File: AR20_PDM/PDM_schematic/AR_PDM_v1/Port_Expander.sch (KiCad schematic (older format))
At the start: 3 parts

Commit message: Fixed issues, controlled components, BOM, see discription
- added acm symbol
- fixed wrongly faced P-mosfets
- I/O expander now sinks led instead of source
- Bill of material mostly done
- Correct address for INA233 chips.
- Now 4 diodes serves as flyback for all mosfets
- Corrected naming scheme for compmonents (everything is not fixed yet)
- Fixed some labels
- altso some minor changes
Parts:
- added C_bypass10, C_bypass9: 100nf, Capacitor_SMD:C_0603_1608Metric, symbol AR20_PDM_v1-rescue:C-Device
- Pullup1, Pullup2: renamed from Pullup?; value 4.7K -> 4K7
- gave numbers to parts that had none: 1
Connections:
- net labels removed: EXPANDER_INT
- wire segments 4 -> 8
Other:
- note added: "Close to PIN"
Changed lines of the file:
@@
 $Descr A4 11693 8268
 encoding utf-8
-Sheet 13 13
+Sheet 12 13
 Title ""
 Date ""
@@
 Comment4 ""
 $EndDescr
-Text HLabel 4000 4075 0    50   Output ~ 0
+Text HLabel 4000 4075 0    50   Input ~ 0
 COIL_INJECTOR_Fault
-Text HLabel 4750 4875 2    50   Output ~ 0
+Text HLabel 4750 4875 2    50   Input ~ 0
 FUEL_PUMP_Fault
-Text HLabel 4000 4775 0    50   Output ~ 0
+Text HLabel 4000 4775 0    50   Input ~ 0
 P7_Fault
-Text HLabel 4000 4675 0    50   Output ~ 0
+Text HLabel 4000 4675 0    50   Input ~ 0
 P6_Fault
-Text HLabel 4000 4575 0    50   Output ~ 0
+Text HLabel 4000 4575 0    50   Input ~ 0
 P5_Fault
-Text HLabel 4000 4475 0    50   Output ~ 0
+Text HLabel 4000 4475 0    50   Input ~ 0
 P4_Fault
-Text HLabel 4000 4375 0    50   Output ~ 0
+Text HLabel 4000 4375 0    50   Input ~ 0
 P3_Fault
-Text HLabel 4000 4175 0    50   Output ~ 0
+Text HLabel 4000 4175 0    50   Input ~ 0
 P1_Fault
-Text HLabel 4000 4275 0    50   Output ~ 0
+Text HLabel 4000 4275 0    50   Input ~ 0
 P2_Fault
 Text HLabel 4750 4775 2    50   Output ~ 0
@@
 AR Path="/5DE4D361/5E218A64" Ref="#PWR?"  Part="1"
 AR Path="/5E218A64" Ref="#PWR?"  Part="1"
-AR Path="/5E1AEC18/5E218A64" Ref="#PWR?"  Part="1"
-F 0 "#PWR?" H 4000 4625 50  0001 C CNN
+AR Path="/5E1AEC18/5E218A64" Ref="#PWR091"  Part="1"
+F 0 "#PWR091" H 4000 4625 50  0001 C CNN
 F 1 "GND" V 4000 4675 50  0000 C CNN
 F 2 "" H 4000 4875 50  0001 C CNN
@@
 Text HLabel 4750 3875 2    50   Input ~ 0
 SDA
-Text HLabel 4750 3775 2    50   Input ~ 0
-VCC_5v
-$Comp
-L AR20_PDM_v1-rescue:TCA6416A-PortExpander U?
+Text HLabel 5025 3775 2    50   Input ~ 0
+VCC_5v
+$Comp
+L AR20_PDM_v1-rescue:TCA6416A-PortExpander U12
 U 1 1 5E21A7B6
 P 4350 5025
-F 0 "U?" H 4375 6500 50  0000 C CNN
+F 0 "U12" H 4375 6500 50  0000 C CNN
 F 1 "TCA6416A-PortExpander" H 4375 6409 50  0000 C CNN
 F 2 "" H 4350 5025 50  0001 C CNN
@@
 VCC_5v
 $Comp
-L AR20_PDM_v1-rescue:R-Device R_s?
+L AR20_PDM_v1-rescue:R-Device Pullup?
 U 1 1 5E2206AE
 P 3875 3625
-AR Path="/5DA89415/5E2206AE" Ref="R_s?"  Part="1"
-AR Path="/5DA8920B/5E2206AE" Ref="R_s?"  Part="1"
-AR Path="/5E2546F2/5E2206AE" Ref="R_s?"  Part="1"
-AR Path="/5E1AEC18/5E2206AE" Ref="Pullup?"  Part="1"
-F 0 "Pullup?" V 3668 3625 50  0000 C CNN
-F 1 "4.7K" V 3759 3625 50  0000 C CNN
+AR Path="/5DA89415/5E2206AE" Ref="Pullup?"  Part="1"
+AR Path="/5DA8920B/5E2206AE" Ref="Pullup?"  Part="1"
+AR Path="/5E2546F2/5E2206AE" Ref="Pullup?"  Part="1"
+AR Path="/5E1AEC18/5E2206AE" Ref="Pullup2"  Part="1"
+F 0 "Pullup2" V 3668 3625 50  0000 C CNN
+F 1 "4K7" V 3759 3625 50  0000 C CNN
 F 2 "" V 3805 3625 50  0001 C CNN
 F 3 "~" H 3875 3625 50  0001 C CNN
@@
 Wire Wire Line
 	4000 3775 3875 3775
-Connection ~ 3875 3775
-Text HLabel 4000 3875 0    50   Input ~ 0
+Text HLabel 2575 3875 0    50   Input ~ 0
 VCC_5v
 Text HLabel 3575 3450 1    50   Input ~ 0
@@
 AR Path="/5DA8920B/5E228956" Ref="Pullup?"  Part="1"
 AR Path="/5E2546F2/5E228956" Ref="Pullup?"  Part="1"
-AR Path="/5E1AEC18/5E228956" Ref="Pullup?"  Part="1"
-F 0 "Pullup?" V 3368 3600 50  0000 C CNN
-F 1 "4.7K" V 3459 3600 50  0000 C CNN
+AR Path="/5E1AEC18/5E228956" Ref="Pullup1"  Part="1"
+F 0 "Pullup1" V 3368 3600 50  0000 C CNN
+F 1 "4K7" V 3459 3600 50  0000 C CNN
 F 2 "" V 3505 3600 50  0001 C CNN
 F 3 "~" H 3575 3600 50  0001 C CNN
@@
 Wire Wire Line
 	3575 3975 4000 3975
-Wire Wire Line
-	3200 3775 3875 3775
-Text HLabel 3200 3775 0    50   Input ~ 0
-EXPANDER_INT
 Text Notes 5150 3950 0    50   ~ 0
 ADDR to gnd, i2c Address: 0100000
@@
 AR Path="/5DE4D361/5E22B252" Ref="#PWR?"  Part="1"
 AR Path="/5E22B252" Ref="#PWR?"  Part="1"
-AR Path="/5E1AEC18/5E22B252" Ref="#PWR?"  Part="1"
-F 0 "#PWR?" H 4750 3825 50  0001 C CNN
+AR Path="/5E1AEC18/5E22B252" Ref="#PWR092"  Part="1"
+F 0 "#PWR092" H 4750 3825 50  0001 C CNN
 F 1 "GND" V 4750 3875 50  0000 C CNN
 F 2 "" H 4750 4075 50  0001 C CNN
@@
 	0    -1   -1   0
 $EndComp
+$Comp
+L AR20_PDM_v1-rescue:C-Device C_bypass?
+U 1 1 5E21FC4A
+P 2600 4100
+AR Path="/5DA89415/5E21FC4A" Ref="C_bypass?"  Part="1"
+AR Path="/5DEB10A1/5E21FC4A" Ref="C_bypass?"  Part="1"
+AR Path="/5DEB20EA/5E21FC4A" Ref="C_bypass?"  Part="1"
+AR Path="/5E0E4725/5E21FC4A" Ref="C_bypass?"  Part="1"
+AR Path="/5E0E4A93/5E21FC4A" Ref="C_bypass?"  Part="1"
+AR Path="/5E0E4EB5/5E21FC4A" Ref="C_bypass?"  Part="1"
+AR Path="/5E0E5304/5E21FC4A" Ref="C_bypass?"  Part="1"
+AR Path="/5E0E594B/5E21FC4A" Ref="C_bypass?"  Part="1"
+AR Path="/5E0E607C/5E21FC4A" Ref="C_bypass?"  Part="1"
+AR Path="/5E0FB5C8/5E21FC4A" Ref="C_bypass?"  Part="1"
+AR Path="/5E0FBBBD/5E21FC4A" Ref="C_bypass?"  Part="1"
+AR Path="/5E0FC3A2/5E21FC4A" Ref="C_bypass?"  Part="1"
+AR Path="/5E0FCFDC/5E21FC4A" Ref="C_bypass?"  Part="1"
+AR Path="/5E0FDCCC/5E21FC4A" Ref="C_bypass?"  Part="1"
+AR Path="/5E10174B/5E21FC4A" Ref="C_bypass?"  Part="1"
+AR Path="/5E1AEC18/5E21FC4A" Ref="C_bypass9"  Part="1"
+F 0 "C_bypass9" V 2348 4100 50  0000 C CNN
+F 1 "100nf" V 2439 4100 50  0000 C CNN
+F 2 "Capacitor_SMD:C_0603_1608Metric" H 2638 3950 50  0001 C CNN
+F 3 "~" H 2600 4100 50  0001 C CNN
+	1    2600 4100
+	1    0    0    -1
+$EndComp
+$Comp
+L AR20_PDM_v1-rescue:GND-power #PWR?
+U 1 1 5E21FC50
+P 2600 4250
+AR Path="/5DA89415/5E21FC50" Ref="#PWR?"  Part="1"
+AR Path="/5DEB10A1/5E21FC50" Ref="#PWR?"  Part="1"
+AR Path="/5DEB20EA/5E21FC50" Ref="#PWR?"  Part="1"
+AR Path="/5E0E4725/5E21FC50" Ref="#PWR?"  Part="1"
+AR Path="/5E0E4A93/5E21FC50" Ref="#PWR?"  Part="1"
+AR Path="/5E0E4EB5/5E21FC50" Ref="#PWR?"  Part="1"
+AR Path="/5E0E5304/5E21FC50" Ref="#PWR?"  Part="1"
+AR Path="/5E0E594B/5E21FC50" Ref="#PWR?"  Part="1"
+AR Path="/5E0E607C/5E21FC50" Ref="#PWR?"  Part="1"
+AR Path="/5E0FB5C8/5E21FC50" Ref="#PWR?"  Part="1"
+AR Path="/5E0FBBBD/5E21FC50" Ref="#PWR?"  Part="1"
+AR Path="/5E0FC3A2/5E21FC50" Ref="#PWR?"  Part="1"
+AR Path="/5E0FCFDC/5E21FC50" Ref="#PWR?"  Part="1"
+AR Path="/5E0FDCCC/5E21FC50" Ref="#PWR?"  Part="1"
+AR Path="/5E10174B/5E21FC50" Ref="#PWR?"  Part="1"
+AR Path="/5E1AEC18/5E21FC50" Ref="#PWR090"  Part="1"
+F 0 "#PWR090" H 2600 4000 50  0001 C CNN
+F 1 "GND" V 2605 4122 50  0000 R CNN
+F 2 "" H 2600 4250 50  0001 C CNN
+F 3 "" H 2600 4250 50  0001 C CNN
+	1    2600 4250
+	1    0    0    -1
+$EndComp
+Text Notes 2625 4000 0    50   ~ 10
+Close to PIN
+Wire Wire Line
+	4000 3875 2600 3875
+Wire Wire Line
+	2600 3950 2600 3875
+Connection ~ 2600 3875
+Wire Wire Line
+	2600 3875 2575 3875
+$Comp
+L AR20_PDM_v1-rescue:C-Device C_bypass?
+U 1 1 5E222000
+P 5025 3500
+AR Path="/5DA89415/5E222000" Ref="C_bypass?"  Part="1"
+AR Path="/5DEB10A1/5E222000" Ref="C_bypass?"  Part="1"
+AR Path="/5DEB20EA/5E222000" Ref="C_bypass?"  Part="1"
+AR Path="/5E0E4725/5E222000" Ref="C_bypass?"  Part="1"
+AR Path="/5E0E4A93/5E222000" Ref="C_bypass?"  Part="1"
+AR Path="/5E0E4EB5/5E222000" Ref="C_bypass?"  Part="1"
+AR Path="/5E0E5304/5E222000" Ref="C_bypass?"  Part="1"
+AR Path="/5E0E594B/5E222000" Ref="C_bypass?"  Part="1"
+AR Path="/5E0E607C/5E222000" Ref="C_bypass?"  Part="1"
+AR Path="/5E0FB5C8/5E222000" Ref="C_bypass?"  Part="1"
+AR Path="/5E0FBBBD/5E222000" Ref="C_bypass?"  Part="1"
+AR Path="/5E0FC3A2/5E222000" Ref="C_bypass?"  Part="1"
+AR Path="/5E0FCFDC/5E222000" Ref="C_bypass?"  Part="1"
+AR Path="/5E0FDCCC/5E222000" Ref="C_bypass?"  Part="1"
+AR Path="/5E10174B/5E222000" Ref="C_bypass?"  Part="1"
+AR Path="/5E1AEC18/5E222000" Ref="C_bypass10"  Part="1"
+F 0 "C_bypass10" V 4773 3500 50  0000 C CNN
+F 1 "100nf" V 4864 3500 50  0000 C CNN
+F 2 "Capacitor_SMD:C_0603_1608Metric" H 5063 3350 50  0001 C CNN
+F 3 "~" H 5025 3500 50  0001 C CNN
+	1    5025 3500
+	-1   0    0    1
+$EndComp
+$Comp
+L AR20_PDM_v1-rescue:GND-power #PWR?
+U 1 1 5E222006
+P 5025 3350
+AR Path="/5DA89415/5E222006" Ref="#PWR?"  Part="1"
+AR Path="/5DEB10A1/5E222006" Ref="#PWR?"  Part="1"
+AR Path="/5DEB20EA/5E222006" Ref="#PWR?"  Part="1"
+AR Path="/5E0E4725/5E222006" Ref="#PWR?"  Part="1"
+AR Path="/5E0E4A93/5E222006" Ref="#PWR?"  Part="1"
+AR Path="/5E0E4EB5/5E222006" Ref="#PWR?"  Part="1"
+AR Path="/5E0E5304/5E222006" Ref="#PWR?"  Part="1"
+AR Path="/5E0E594B/5E222006" Ref="#PWR?"  Part="1"
+AR Path="/5E0E607C/5E222006" Ref="#PWR?"  Part="1"
+AR Path="/5E0FB5C8/5E222006" Ref="#PWR?"  Part="1"
+AR Path="/5E0FBBBD/5E222006" Ref="#PWR?"  Part="1"
+AR Path="/5E0FC3A2/5E222006" Ref="#PWR?"  Part="1"
+AR Path="/5E0FCFDC/5E222006" Ref="#PWR?"  Part="1"
+AR Path="/5E0FDCCC/5E222006" Ref="#PWR?"  Part="1"
+AR Path="/5E10174B/5E222006" Ref="#PWR?"  Part="1"
+AR Path="/5E1AEC18/5E222006" Ref="#PWR093"  Part="1"
+F 0 "#PWR093" H 5025 3100 50  0001 C CNN
+F 1 "GND" V 5030 3222 50  0000 R CNN
+F 2 "" H 5025 3350 50  0001 C CNN
+F 3 "" H 5025 3350 50  0001 C CNN
+	1    5025 3350
+	-1   0    0    1
+$EndComp
+Wire Wire Line
+	5025 3650 5025 3775
+Wire Wire Line
+	4750 3775 5025 3775
 $EndSCHEMATC

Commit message: PCB design, and issue fixing, work in progress
- Error fixed: Mux mosfet resistor change to ground
- Open drain output added on phase 6, for engine blipping purpose
- Most of pcb symbols and footprints are finished, including main connector
- PCB is change from 1oz to 2oz copper layer, for easier routing.
- Basic Draft of pcb is done, for now.
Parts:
- Pullup1, Pullup2: footprint (none) -> Resistor_SMD:R_0603_1608Metric
- U12: footprint (none) -> AR_PDM_v1:SOP65P640X120-24N
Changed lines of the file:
@@
 F 0 "U12" H 4375 6500 50  0000 C CNN
 F 1 "TCA6416A-PortExpander" H 4375 6409 50  0000 C CNN
-F 2 "" H 4350 5025 50  0001 C CNN
+F 2 "AR_PDM_v1:SOP65P640X120-24N" H 4350 5025 50  0001 C CNN
 F 3 "" H 4350 5025 50  0001 C CNN
 	1    4350 5025
@@
 F 0 "Pullup2" V 3668 3625 50  0000 C CNN
 F 1 "4K7" V 3759 3625 50  0000 C CNN
-F 2 "" V 3805 3625 50  0001 C CNN
+F 2 "Resistor_SMD:R_0603_1608Metric" V 3805 3625 50  0001 C CNN
 F 3 "~" H 3875 3625 50  0001 C CNN
 	1    3875 3625
@@
 F 0 "Pullup1" V 3368 3600 50  0000 C CNN
 F 1 "4K7" V 3459 3600 50  0000 C CNN
-F 2 "" V 3505 3600 50  0001 C CNN
+F 2 "Resistor_SMD:R_0603_1608Metric" V 3505 3600 50  0001 C CNN
 F 3 "~" H 3575 3600 50  0001 C CNN
 	1    3575 3600

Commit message: First Complete Draft of PCB and schematics, - minus see discription
- missing correct smd switch header
- missing correct main power plug
- tweeks still needs to be done
- Extra inspection of schematics pending
- proper, in depth quiality controll of pcb work pending
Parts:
- removed U12: TCA6416A-PortExpander, AR_PDM_v1:SOP65P640X120-24N, symbol AR20_PDM_v1-rescue:TCA6416A-PortExpander
- added U12: TCA6424ARGJR, AR_PDM_v1:QFN50P500X500X60-33N, symbol TCA6424ARGJR:TCA6424ARGJR
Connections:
- net labels added: COIL_INJECTOR_Alert, FP_Alert, FP_ENABLE_ACM
- wire segments 8 -> 9
- no-connect marks 0 -> 6
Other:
- note removed: "Close to PIN"
- moved on the sheet: C_bypass10, Pullup1, Pullup2

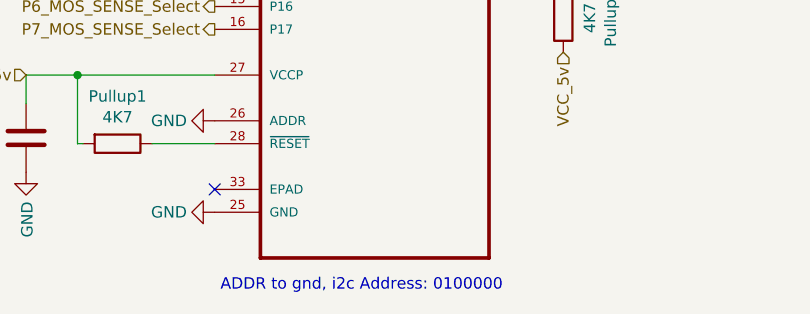
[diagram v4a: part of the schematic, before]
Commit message: Finilizing the desing, some few missing components
- Increased the size to accommodate mounting holes
- Fixed wrong p mos pin out, due to wrong schematics drawing
- Done alot of tweeeks 
- Button connector still missing.
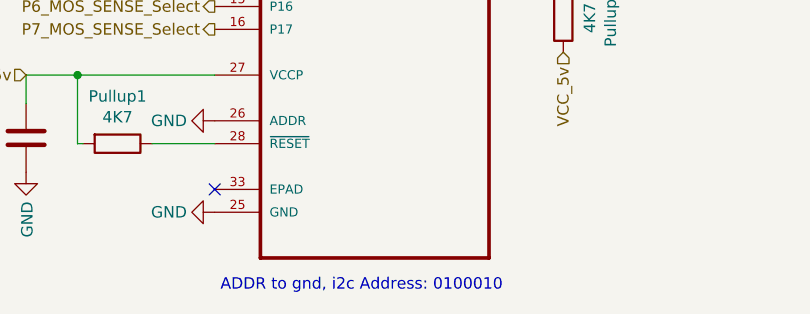
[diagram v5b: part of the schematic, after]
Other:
- note added: "ADDR to gnd, i2c Address: 0100010"
- note removed: "ADDR to gnd, i2c Address: 0100000"
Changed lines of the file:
@@
 $EndComp
 Text Notes 6850 5625 0    50   ~ 0
-ADDR to gnd, i2c Address: 0100000
+ADDR to gnd, i2c Address: 0100010
 $Comp
 L AR20_PDM_v1-rescue:C-Device C_bypass?

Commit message: Alpha version DONE! - Gerber files generated
- Tweeked
- checked and re cheked
- added all missing components
- Created a really nice silkscreen
- Ready To Test
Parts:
- renumbered C_bypass10 to C42, C_bypass9 to C43, Pullup1 to R46, Pullup2 to R47, U12 to U9
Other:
- moved on the sheet: C42, C43, R46, R47, U9

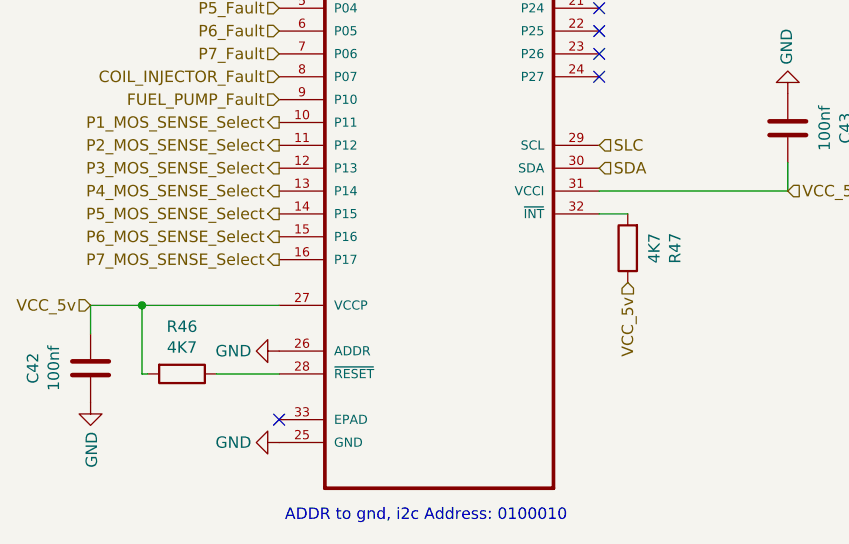
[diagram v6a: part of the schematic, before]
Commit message: Fixed wrong resistors, mos sense. Gerber files updated
- removed all R_is_protection resistors on each mosfet line
- added one R_is_protection resistors to mos_sense_all
ps, mux N-fets, does not need overvoltage protection. 60 volt tolerant.
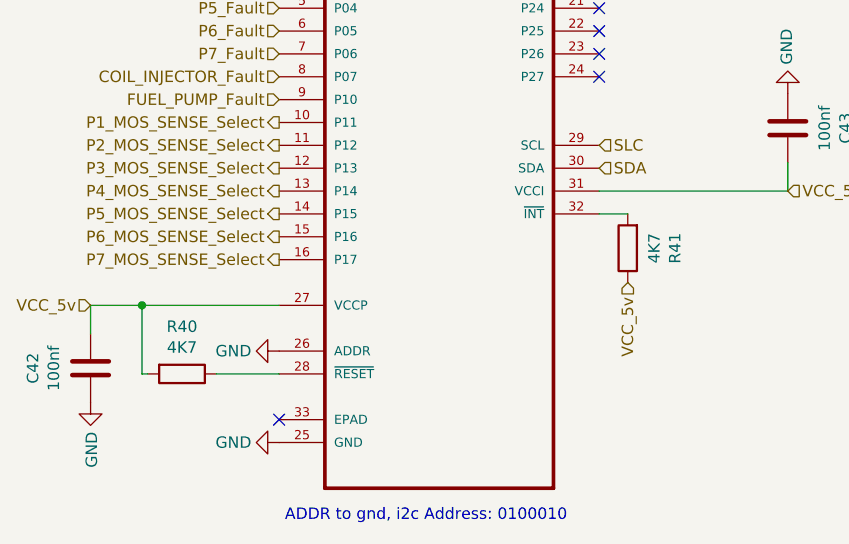
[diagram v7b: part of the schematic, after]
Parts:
- renumbered R46 to R40, R47 to R41
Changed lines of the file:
@@
 AR Path="/5DA8920B/5E2206AE" Ref="R?"  Part="1"
 AR Path="/5E2546F2/5E2206AE" Ref="R?"  Part="1"
-AR Path="/5E1AEC18/5E2206AE" Ref="R47"  Part="1"
-F 0 "R47" V 6393 4100 50  0000 C CNN
+AR Path="/5E1AEC18/5E2206AE" Ref="R41"  Part="1"
+F 0 "R41" V 6393 4100 50  0000 C CNN
 F 1 "4K7" V 6484 4100 50  0000 C CNN
 F 2 "Resistor_SMD:R_0603_1608Metric" V 6530 4100 50  0001 C CNN
@@
 AR Path="/5DA8920B/5E228956" Ref="R?"  Part="1"
 AR Path="/5E2546F2/5E228956" Ref="R?"  Part="1"
-AR Path="/5E1AEC18/5E228956" Ref="R46"  Part="1"
-F 0 "R46" V 4443 4650 50  0000 C CNN
+AR Path="/5E1AEC18/5E228956" Ref="R40"  Part="1"
+F 0 "R40" V 4443 4650 50  0000 C CNN
 F 1 "4K7" V 4534 4650 50  0000 C CNN
 F 2 "Resistor_SMD:R_0603_1608Metric" V 4580 4650 50  0001 C CNN

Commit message: Major redesign. schematics completed, PCB work in progress
-TODO : A proper changelog file. Where all changes will apear 
- Redesigned schematics to accommodate errors in the improvement list
- More detail in ALPHA improvement list
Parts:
- U9: symbol TCA6424ARGJR:TCA6424ARGJR -> AR20_PDM_v1-rescue:TCA6424ARGJR
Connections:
- net COIL_INJECTOR_Alert: no longer names the net of U9.18 (P21)
- net FP_Alert: no longer names the net of U9.17 (P20)
- net P1_MOS_SENSE_Select renamed Mux_select_A2
- net P2_MOS_SENSE_Select renamed Mux_select_A1
- net P3_MOS_SENSE_Select renamed Mux_select_A0
- net P4_MOS_SENSE_Select renamed Mux_enable
- net P5_MOS_SENSE_Select: no longer names the net of U9.14 (P15)
- net P6_MOS_SENSE_Select: no longer names the net of U9.15 (P16)
- net P7_MOS_SENSE_Select: no longer names the net of U9.16 (P17)
- no-connect marks 6 -> 11
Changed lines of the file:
@@
 $Descr A4 11693 8268
 encoding utf-8
-Sheet 10 13
+Sheet 10 14
 Title ""
 Date ""
@@
 Comment4 ""
 $EndDescr
-Text HLabel 5075 3450 0    50   Input ~ 0
-FUEL_PUMP_Fault
-Text HLabel 5075 3550 0    50   Output ~ 0
-P1_MOS_SENSE_Select
-Text HLabel 5075 3650 0    50   Output ~ 0
-P2_MOS_SENSE_Select
-Text HLabel 5075 3750 0    50   Output ~ 0
-P3_MOS_SENSE_Select
-Text HLabel 5075 3850 0    50   Output ~ 0
-P4_MOS_SENSE_Select
-Text HLabel 5075 3950 0    50   Output ~ 0
-P5_MOS_SENSE_Select
-Text HLabel 5075 4050 0    50   Output ~ 0
-P6_MOS_SENSE_Select
-Text HLabel 5075 4150 0    50   Output ~ 0
-P7_MOS_SENSE_Select
 Text HLabel 6475 3650 2    50   Input ~ 0
 SLC
@@
 	0    1    1    0
 $EndComp
-Text HLabel 5075 3350 0    50   Input ~ 0
-COIL_INJECTOR_Fault
 Text HLabel 5075 3250 0    50   Input ~ 0
 P7_Fault
@@
 Text HLabel 5075 2750 0    50   Input ~ 0
 P2_Fault
-Text HLabel 6475 2650 2    50   Input ~ 0
-FP_Alert
-Text HLabel 6475 2750 2    50   Input ~ 0
-COIL_INJECTOR_Alert
 NoConn ~ 5075 4850
 Wire Wire Line
@@
 $EndComp
 $Comp
-L TCA6424ARGJR:TCA6424ARGJR U9
+L AR20_PDM_v1-rescue:TCA6424ARGJR U9
 U 1 1 5E280A9C
 P 5775 3650
+AR Path="/5E280A9C" Ref="U9"  Part="1"
+AR Path="/5E1AEC18/5E280A9C" Ref="U9"  Part="1"
 F 0 "U9" H 5775 5020 50  0000 C CNN
 F 1 "TCA6424ARGJR" H 5775 4929 50  0000 C CNN
@@
 NoConn ~ 6475 3150
 NoConn ~ 6475 3350
+Text HLabel 5075 3750 0    50   Input ~ 0
+Mux_select_A0
+Text HLabel 5075 3650 0    50   Input ~ 0
+Mux_select_A1
+Text HLabel 5075 3550 0    50   Input ~ 0
+Mux_select_A2
+Text HLabel 5075 3850 0    50   Input ~ 0
+Mux_enable
+NoConn ~ 5075 3950
+NoConn ~ 5075 4050
+NoConn ~ 5075 4150
+Text HLabel 5075 3350 0    50   Input ~ 0
+COIL_INJECTOR_Fault
+Text HLabel 5075 3450 0    50   Input ~ 0
+FUEL_PUMP_Fault
+NoConn ~ 6475 2750
+NoConn ~ 6475 2650
 $EndSCHEMATC
